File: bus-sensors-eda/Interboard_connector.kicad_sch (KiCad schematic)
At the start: 1 part, among them J1 Conn_02x20_Odd_Even

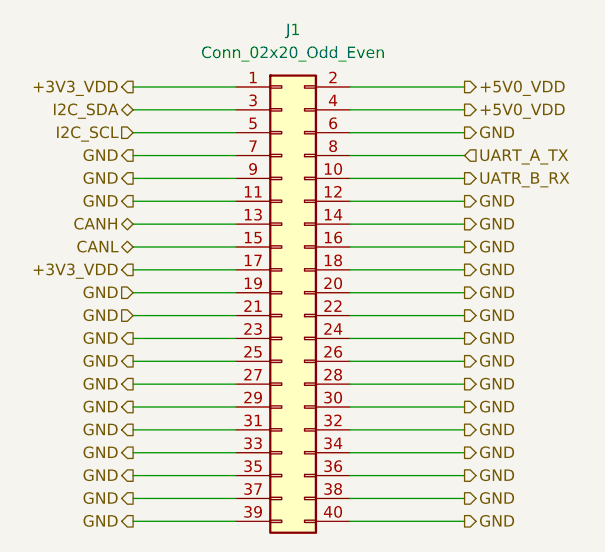
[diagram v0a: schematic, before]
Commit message: courtyards and silkscreens correction
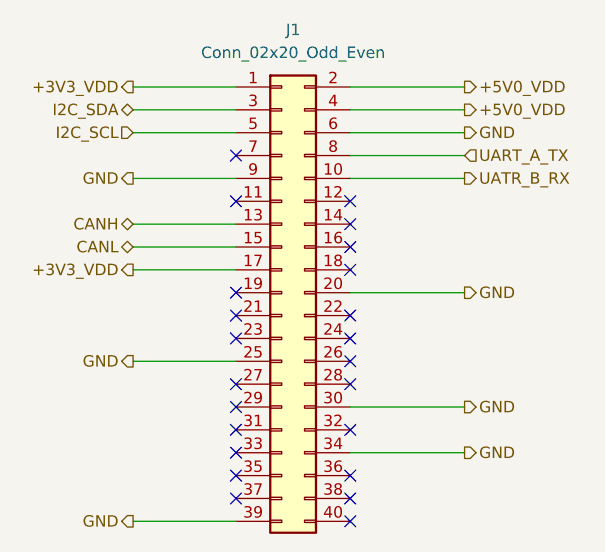
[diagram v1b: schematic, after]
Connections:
- net GND: no longer J1.11 (Pin_11), J1.12 (Pin_12), J1.14 (Pin_14), J1.16 (Pin_16), J1.18 (Pin_18), J1.19 (Pin_19), J1.21 (Pin_21), J1.22 (Pin_22), J1.23 (Pin_23), J1.24 (Pin_24), J1.26 (Pin_26), J1.27 (Pin_27), J1.28 (Pin_28), J1.29 (Pin_29), J1.31 (Pin_31), J1.32 (Pin_32), J1.33 (Pin_33), J1.35 (Pin_35), J1.36 (Pin_36), J1.37 (Pin_37), J1.38 (Pin_38), J1.40 (Pin_40), J1.7 (Pin_7)
- no-connect marks 0 -> 23
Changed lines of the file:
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@@
     (date "2022-01-27")
   )
-  (wire (pts (xy 130.81 93.98) (xy 143.51 93.98))
-    (stroke (width 0) (type default) (color 0 0 0 0))
-  )
+  (no_connect (at 130.81 76.2))
+  (no_connect (at 130.81 78.74))
+  (no_connect (at 130.81 81.28))
+  (no_connect (at 118.11 76.2))
+  (no_connect (at 130.81 111.76))
+  (no_connect (at 118.11 101.6))
+  (no_connect (at 118.11 104.14))
+  (no_connect (at 118.11 106.68))
+  (no_connect (at 118.11 109.22))
+  (no_connect (at 130.81 83.82))
+  (no_connect (at 130.81 88.9))
+  (no_connect (at 118.11 71.12))
+  (no_connect (at 118.11 86.36))
+  (no_connect (at 118.11 88.9))
+  (no_connect (at 130.81 91.44))
+  (no_connect (at 130.81 93.98))
+  (no_connect (at 118.11 91.44))
+  (no_connect (at 118.11 96.52))
+  (no_connect (at 118.11 99.06))
+  (no_connect (at 130.81 96.52))
+  (no_connect (at 130.81 101.6))
+  (no_connect (at 130.81 106.68))
+  (no_connect (at 130.81 109.22))
   (wire (pts (xy 130.81 68.58) (xy 143.51 68.58))
     (stroke (width 0) (type default) (color 0 0 0 0))
@@
     (stroke (width 0) (type default) (color 0 0 0 0))
   )
-  (wire (pts (xy 130.81 111.76) (xy 143.51 111.76))
-    (stroke (width 0) (type default) (color 0 0 0 0))
-  )
   (wire (pts (xy 106.68 93.98) (xy 118.11 93.98))
     (stroke (width 0) (type default) (color 0 0 0 0))
   )
-  (wire (pts (xy 106.68 104.14) (xy 118.11 104.14))
-    (stroke (width 0) (type default) (color 0 0 0 0))
-  )
   (wire (pts (xy 106.68 68.58) (xy 118.11 68.58))
-    (stroke (width 0) (type default) (color 0 0 0 0))
-  )
-  (wire (pts (xy 106.68 106.68) (xy 118.11 106.68))
-    (stroke (width 0) (type default) (color 0 0 0 0))
-  )
-  (wire (pts (xy 106.68 71.12) (xy 118.11 71.12))
-    (stroke (width 0) (type default) (color 0 0 0 0))
-  )
-  (wire (pts (xy 130.81 91.44) (xy 143.51 91.44))
     (stroke (width 0) (type default) (color 0 0 0 0))
   )
@@
     (stroke (width 0) (type default) (color 0 0 0 0))
   )
-  (wire (pts (xy 130.81 81.28) (xy 143.51 81.28))
-    (stroke (width 0) (type default) (color 0 0 0 0))
-  )
-  (wire (pts (xy 130.81 106.68) (xy 143.51 106.68))
-    (stroke (width 0) (type default) (color 0 0 0 0))
-  )
   (wire (pts (xy 106.68 111.76) (xy 118.11 111.76))
     (stroke (width 0) (type default) (color 0 0 0 0))
   )
-  (wire (pts (xy 106.68 101.6) (xy 118.11 101.6))
-    (stroke (width 0) (type default) (color 0 0 0 0))
-  )
   (wire (pts (xy 130.81 66.04) (xy 143.51 66.04))
-    (stroke (width 0) (type default) (color 0 0 0 0))
-  )
-  (wire (pts (xy 106.68 86.36) (xy 118.11 86.36))
-    (stroke (width 0) (type default) (color 0 0 0 0))
-  )
-  (wire (pts (xy 130.81 76.2) (xy 143.51 76.2))
-    (stroke (width 0) (type default) (color 0 0 0 0))
-  )
-  (wire (pts (xy 130.81 101.6) (xy 143.51 101.6))
     (stroke (width 0) (type default) (color 0 0 0 0))
   )
@@
     (stroke (width 0) (type default) (color 0 0 0 0))
   )
-  (wire (pts (xy 130.81 88.9) (xy 143.51 88.9))
-    (stroke (width 0) (type default) (color 0 0 0 0))
-  )
-  (wire (pts (xy 130.81 83.82) (xy 143.51 83.82))
-    (stroke (width 0) (type default) (color 0 0 0 0))
-  )
   (wire (pts (xy 106.68 83.82) (xy 118.11 83.82))
     (stroke (width 0) (type default) (color 0 0 0 0))
@@
     (stroke (width 0) (type default) (color 0 0 0 0))
   )
-  (wire (pts (xy 106.68 76.2) (xy 118.11 76.2))
-    (stroke (width 0) (type default) (color 0 0 0 0))
-  )
-  (wire (pts (xy 106.68 96.52) (xy 118.11 96.52))
-    (stroke (width 0) (type default) (color 0 0 0 0))
-  )
-  (wire (pts (xy 106.68 109.22) (xy 118.11 109.22))
-    (stroke (width 0) (type default) (color 0 0 0 0))
-  )
   (wire (pts (xy 106.68 63.5) (xy 118.11 63.5))
-    (stroke (width 0) (type default) (color 0 0 0 0))
-  )
-  (wire (pts (xy 106.68 88.9) (xy 118.11 88.9))
     (stroke (width 0) (type default) (color 0 0 0 0))
   )
@@
     (stroke (width 0) (type default) (color 0 0 0 0))
   )
-  (wire (pts (xy 106.68 91.44) (xy 118.11 91.44))
-    (stroke (width 0) (type default) (color 0 0 0 0))
-  )
   (wire (pts (xy 106.68 81.28) (xy 118.11 81.28))
-    (stroke (width 0) (type default) (color 0 0 0 0))
-  )
-  (wire (pts (xy 130.81 109.22) (xy 143.51 109.22))
-    (stroke (width 0) (type default) (color 0 0 0 0))
-  )
-  (wire (pts (xy 106.68 99.06) (xy 118.11 99.06))
-    (stroke (width 0) (type default) (color 0 0 0 0))
-  )
-  (wire (pts (xy 130.81 78.74) (xy 143.51 78.74))
-    (stroke (width 0) (type default) (color 0 0 0 0))
-  )
-  (wire (pts (xy 130.81 96.52) (xy 143.51 96.52))
     (stroke (width 0) (type default) (color 0 0 0 0))
   )
   (wire (pts (xy 106.68 73.66) (xy 118.11 73.66))
     (stroke (width 0) (type default) (color 0 0 0 0))
-  )
-  (hierarchical_label "GND" (shape input) (at 106.68 86.36 180)
-    (effects (font (size 1.27 1.27)) (justify right))
   )
   (hierarchical_label "CANH" (shape bidirectional) (at 106.68 78.74 180)
@@
     (effects (font (size 1.27 1.27)) (justify right))
   )
-  (hierarchical_label "GND" (shape output) (at 106.68 104.14 180)
-    (effects (font (size 1.27 1.27)) (justify right))
-  )
-  (hierarchical_label "GND" (shape output) (at 143.51 101.6 0)
-    (effects (font (size 1.27 1.27)) (justify left))
-  )
   (hierarchical_label "GND" (shape output) (at 106.68 73.66 180)
     (effects (font (size 1.27 1.27)) (justify right))
@@
     (effects (font (size 1.27 1.27)) (justify right))
   )
-  (hierarchical_label "GND" (shape output) (at 143.51 111.76 0)
-    (effects (font (size 1.27 1.27)) (justify left))
-  )
-  (hierarchical_label "GND" (shape output) (at 143.51 76.2 0)
-    (effects (font (size 1.27 1.27)) (justify left))
-  )
   (hierarchical_label "GND" (shape output) (at 143.51 68.58 0)
     (effects (font (size 1.27 1.27)) (justify left))
@@
     (effects (font (size 1.27 1.27)) (justify right))
   )
-  (hierarchical_label "GND" (shape output) (at 143.51 91.44 0)
-    (effects (font (size 1.27 1.27)) (justify left))
-  )
-  (hierarchical_label "GND" (shape output) (at 143.51 88.9 0)
-    (effects (font (size 1.27 1.27)) (justify left))
-  )
-  (hierarchical_label "GND" (shape input) (at 106.68 88.9 180)
-    (effects (font (size 1.27 1.27)) (justify right))
-  )
-  (hierarchical_label "GND" (shape output) (at 143.51 83.82 0)
-    (effects (font (size 1.27 1.27)) (justify left))
-  )
   (hierarchical_label "+5V0_VDD" (shape output) (at 143.51 63.5 0)
-    (effects (font (size 1.27 1.27)) (justify left))
-  )
-  (hierarchical_label "GND" (shape output) (at 106.68 99.06 180)
-    (effects (font (size 1.27 1.27)) (justify right))
-  )
-  (hierarchical_label "GND" (shape output) (at 143.51 109.22 0)
-    (effects (font (size 1.27 1.27)) (justify left))
-  )
-  (hierarchical_label "GND" (shape output) (at 143.51 78.74 0)
     (effects (font (size 1.27 1.27)) (justify left))
   )
   (hierarchical_label "+5V0_VDD" (shape output) (at 143.51 66.04 0)
     (effects (font (size 1.27 1.27)) (justify left))
-  )
-  (hierarchical_label "GND" (shape output) (at 106.68 106.68 180)
-    (effects (font (size 1.27 1.27)) (justify right))
   )
   (hierarchical_label "GND" (shape output) (at 143.51 104.14 0)
@@
     (effects (font (size 1.27 1.27)) (justify right))
   )
-  (hierarchical_label "GND" (shape output) (at 106.68 71.12 180)
-    (effects (font (size 1.27 1.27)) (justify right))
-  )
-  (hierarchical_label "GND" (shape output) (at 106.68 91.44 180)
-    (effects (font (size 1.27 1.27)) (justify right))
-  )
-  (hierarchical_label "GND" (shape output) (at 106.68 101.6 180)
-    (effects (font (size 1.27 1.27)) (justify right))
-  )
-  (hierarchical_label "GND" (shape output) (at 106.68 76.2 180)
-    (effects (font (size 1.27 1.27)) (justify right))
-  )
-  (hierarchical_label "GND" (shape output) (at 143.51 81.28 0)
-    (effects (font (size 1.27 1.27)) (justify left))
-  )
   (hierarchical_label "GND" (shape output) (at 106.68 93.98 180)
     (effects (font (size 1.27 1.27)) (justify right))
-  )
-  (hierarchical_label "GND" (shape output) (at 143.51 93.98 0)
-    (effects (font (size 1.27 1.27)) (justify left))
-  )
-  (hierarchical_label "GND" (shape output) (at 143.51 106.68 0)
-    (effects (font (size 1.27 1.27)) (justify left))
-  )
-  (hierarchical_label "GND" (shape output) (at 106.68 109.22 180)
-    (effects (font (size 1.27 1.27)) (justify right))
-  )
-  (hierarchical_label "GND" (shape output) (at 143.51 96.52 0)
-    (effects (font (size 1.27 1.27)) (justify left))
   )
   (hierarchical_label "I2C_SDA" (shape bidirectional) (at 106.68 66.04 180)
@@
     (effects (font (size 1.27 1.27)) (justify right))
   )
-  (hierarchical_label "GND" (shape output) (at 106.68 96.52 180)
-    (effects (font (size 1.27 1.27)) (justify right))
-  )
